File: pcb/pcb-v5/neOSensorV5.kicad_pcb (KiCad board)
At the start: 2 copper layers, 49.5 x 49.5 mm, 49 parts, among them J1 Conn_01x04, J2 Conn_01x04, J3 Conn_01x05, J4 Conn_01x05, J5 Conn_01x05, J6 Conn_01x06, Q1 2N7002, SW1 clear, SW2 +, SW3 -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

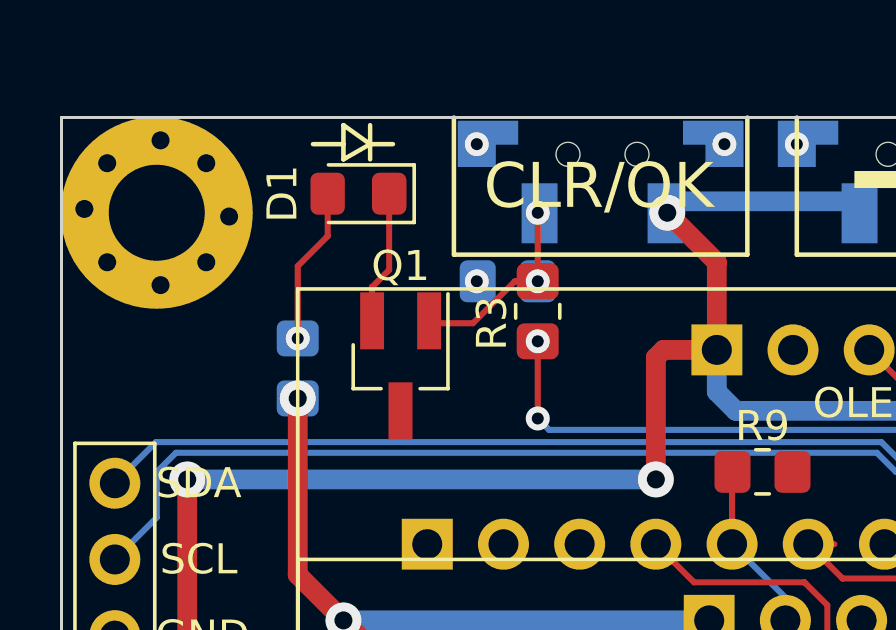
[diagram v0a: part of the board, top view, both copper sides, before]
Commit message: start mods for pcb v5.1
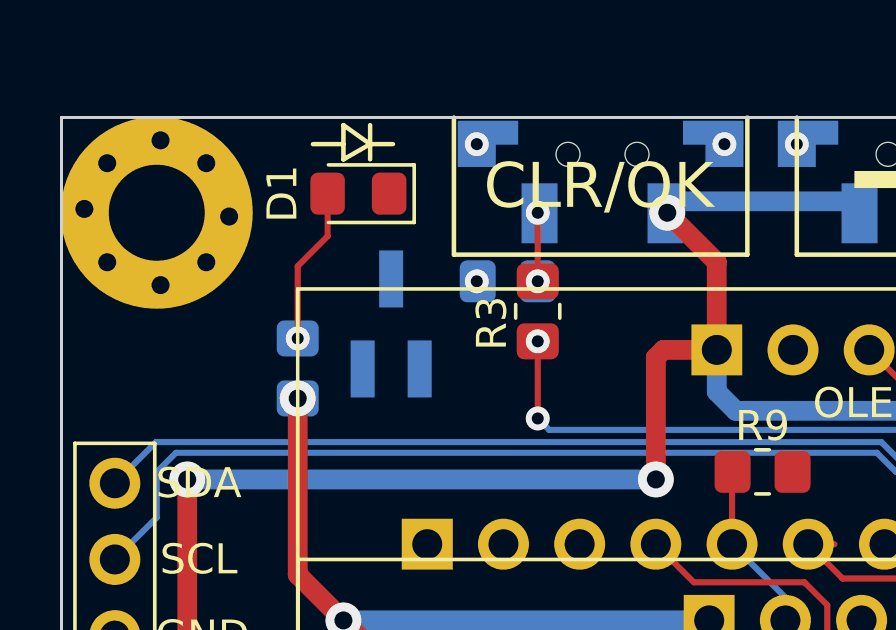
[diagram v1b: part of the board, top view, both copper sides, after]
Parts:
- Q1: moved to B.Cu
- moved Q1 1.43 mm to (36.4, 32.3), turned to 90 degrees
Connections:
- Q1 pad 2: Net-(D1-Pad1) -> GND
- Q1 pad 3: GND -> Net-(D1-Pad1)
- U3 pad 16: +3V3 -> Net-(U3-Pad16)
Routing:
- net Net-(D1-Pad1): track 4.47 -> 0.00 mm
- net Net-(Q1-Pad1): track 6.92 -> 2.69 mm
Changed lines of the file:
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@@
-(kicad_pcb (version 20171130) (host pcbnew 5.1.8-1.fc31)
+(kicad_pcb (version 20171130) (host pcbnew 5.1.5+dfsg1-2build2)
   (general
     (thickness 1.6)
     (drawings 71)
-    (tracks 381)
+    (tracks 374)
     (zones 0)
     (modules 49)
-    (nets 45)
+    (nets 46)
   )
   (page A4)
@@
     (32 B.Adhes user hide)
     (33 F.Adhes user hide)
-    (34 B.Paste user)
-    (35 F.Paste user)
+    (34 B.Paste user hide)
+    (35 F.Paste user hide)
     (36 B.SilkS user)
-    (37 F.SilkS user)
-    (38 B.Mask user)
-    (39 F.Mask user)
-    (40 Dwgs.User user)
+    (37 F.SilkS user hide)
+    (38 B.Mask user hide)
+    (39 F.Mask user hide)
+    (40 Dwgs.User user hide)
     (41 Cmts.User user hide)
     (42 Eco1.User user hide)
@@
   (net 43 "Net-(U3-Pad1)")
   (net 44 "Net-(D1-Pad2)")
+  (net 45 "Net-(U3-Pad16)")
   (net_class Default "This is the default net class."
     (clearance 0.1524)
@@
     (add_net "Net-(U3-Pad12)")
     (add_net "Net-(U3-Pad13)")
+    (add_net "Net-(U3-Pad16)")
     (add_net "Net-(U3-Pad21)")
     (add_net "Net-(U3-Pad22)")
@@
     (add_net GND)
   )
-  (module Package_TO_SOT_SMD:SOT-23_Handsoldering (layer F.Cu)
-    (at 36.703 33.679 270)
+  (module Package_TO_SOT_SMD:SOT-23_Handsoldering (layer B.Cu)
+    (at 36.388 32.282 90)
     (descr "SOT-23, Handsoldering")
     (tags SOT-23)
     (attr smd)
-    (fp_text reference Q1 (at -3.326 0 180) (layer F.SilkS)
-      (effects (font (size 1 1) (thickness 0.15)))
-    )
-    (fp_text value 2N7002 (at 0 2.5 90) (layer F.Fab)
-      (effects (font (size 1 1) (thickness 0.15)))
-    )
-    (fp_line (start 0.76 1.58) (end 0.76 0.65) (layer F.SilkS) (width 0.12))
-    (fp_line (start 0.76 -1.58) (end 0.76 -0.65) (layer F.SilkS) (width 0.12))
-    (fp_line (start -2.7 -1.75) (end 2.7 -1.75) (layer F.CrtYd) (width 0.05))
-    (fp_line (start 2.7 -1.75) (end 2.7 1.75) (layer F.CrtYd) (width 0.05))
-    (fp_line (start 2.7 1.75) (end -2.7 1.75) (layer F.CrtYd) (width 0.05))
-    (fp_line (start -2.7 1.75) (end -2.7 -1.75) (layer F.CrtYd) (width 0.05))
-    (fp_line (start 0.76 -1.58) (end -2.4 -1.58) (layer F.SilkS) (width 0.12))
-    (fp_line (start -0.7 -0.95) (end -0.7 1.5) (layer F.Fab) (width 0.1))
-    (fp_line (start -0.15 -1.52) (end 0.7 -1.52) (layer F.Fab) (width 0.1))
-    (fp_line (start -0.7 -0.95) (end -0.15 -1.52) (layer F.Fab) (width 0.1))
-    (fp_line (start 0.7 -1.52) (end 0.7 1.52) (layer F.Fab) (width 0.1))
-    (fp_line (start -0.7 1.52) (end 0.7 1.52) (layer F.Fab) (width 0.1))
-    (fp_line (start 0.76 1.58) (end -0.7 1.58) (layer F.SilkS) (width 0.12))
-    (fp_text user %R (at 0 0) (layer F.Fab)
-      (effects (font (size 0.5 0.5) (thickness 0.075)))
-    )
-    (pad 3 smd rect (at 1.5 0 270) (size 1.9 0.8) (layers F.Cu F.Paste F.Mask)
-      (net 1 GND))
-    (pad 2 smd rect (at -1.5 0.95 270) (size 1.9 0.8) (layers F.Cu F.Paste F.Mask)
+    (fp_text reference Q1 (at -3.326 0 180) (layer B.SilkS)
+      (effects (font (size 1 1) (thickness 0.15)) (justify mirror))
+    )
+    (fp_text value 2N7002 (at 0 -2.5 270) (layer B.Fab)
+      (effects (font (size 1 1) (thickness 0.15)) (justify mirror))
+    )
+    (fp_line (start 0.76 -1.58) (end 0.76 -0.65) (layer B.SilkS) (width 0.12))
+    (fp_line (start 0.76 1.58) (end 0.76 0.65) (layer B.SilkS) (width 0.12))
+    (fp_line (start -2.7 1.75) (end 2.7 1.75) (layer B.CrtYd) (width 0.05))
+    (fp_line (start 2.7 1.75) (end 2.7 -1.75) (layer B.CrtYd) (width 0.05))
+    (fp_line (start 2.7 -1.75) (end -2.7 -1.75) (layer B.CrtYd) (width 0.05))
+    (fp_line (start -2.7 -1.75) (end -2.7 1.75) (layer B.CrtYd) (width 0.05))
+    (fp_line (start 0.76 1.58) (end -2.4 1.58) (layer B.SilkS) (width 0.12))
+    (fp_line (start -0.7 0.95) (end -0.7 -1.5) (layer B.Fab) (width 0.1))
+    (fp_line (start -0.15 1.52) (end 0.7 1.52) (layer B.Fab) (width 0.1))
+    (fp_line (start -0.7 0.95) (end -0.15 1.52) (layer B.Fab) (width 0.1))
+    (fp_line (start 0.7 1.52) (end 0.7 -1.52) (layer B.Fab) (width 0.1))
+    (fp_line (start -0.7 -1.52) (end 0.7 -1.52) (layer B.Fab) (width 0.1))
+    (fp_line (start 0.76 -1.58) (end -0.7 -1.58) (layer B.SilkS) (width 0.12))
+    (fp_text user %R (at 0 0) (layer B.Fab)
+      (effects (font (size 0.5 0.5) (thickness 0.075)) (justify mirror))
+    )
+    (pad 3 smd rect (at 1.5 0 90) (size 1.9 0.8) (layers B.Cu B.Paste B.Mask)
       (net 6 "Net-(D1-Pad1)"))
-    (pad 1 smd rect (at -1.5 -0.95 270) (size 1.9 0.8) (layers F.Cu F.Paste F.Mask)
+    (pad 2 smd rect (at -1.5 -0.95 90) (size 1.9 0.8) (layers B.Cu B.Paste B.Mask)
+      (net 1 GND))
+    (pad 1 smd rect (at -1.5 0.95 90) (size 1.9 0.8) (layers B.Cu B.Paste B.Mask)
       (net 17 "Net-(Q1-Pad1)"))
     (model ${KISYS3DMOD}/Package_TO_SOT_SMD.3dshapes/SOT-23.wrl
@@
       (net 29 /ADC1_0))
     (pad 16 thru_hole circle (at -12.7 19.05 270) (size 1.7 1.7) (drill 1) (layers *.Cu *.Mask)
-      (net 3 +3V3))
+      (net 45 "Net-(U3-Pad16)"))
     (pad 15 thru_hole circle (at 12.7 19.05 270) (size 1.7 1.7) (drill 1) (layers *.Cu *.Mask)
       (net 5 /SW3))
@@
   (segment (start 71.12 37.592) (end 73.152 39.624) (width 0.2032) (layer F.Cu) (net 5))
   (segment (start 71.12 33.909) (end 71.12 37.592) (width 0.2032) (layer F.Cu) (net 5))
-  (segment (start 35.753 32.179) (end 35.753 31.049) (width 0.2032) (layer F.Cu) (net 6))
-  (segment (start 36.322 30.48) (end 36.322 27.94) (width 0.2032) (layer F.Cu) (net 6))
-  (segment (start 35.753 31.049) (end 36.322 30.48) (width 0.2032) (layer F.Cu) (net 6))
   (segment (start 62.992 37.306) (end 62.865 37.179) (width 0.2032) (layer F.Cu) (net 7))
   (segment (start 62.992 39.624) (end 62.992 37.306) (width 0.2032) (layer F.Cu) (net 7))
@@
   (segment (start 41.275 28.253) (end 41.334 28.194) (width 0.2032) (layer B.Cu) (net 17))
   (segment (start 41.275 28.575) (end 41.275 28.253) (width 0.2032) (layer B.Cu) (net 17))
-  (segment (start 40.513 30.861) (end 41.275 30.861) (width 0.2032) (layer F.Cu) (net 17))
-  (segment (start 39.116 32.258) (end 40.513 30.861) (width 0.2032) (layer F.Cu) (net 17))
-  (segment (start 37.732 32.258) (end 37.653 32.179) (width 0.2032) (layer F.Cu) (net 17))
-  (segment (start 39.116 32.258) (end 37.732 32.258) (width 0.2032) (layer F.Cu) (net 17))
   (via (at 41.275 32.861) (size 0.8) (drill 0.4) (layers F.Cu B.Cu) (net 18))
   (segment (start 41.307 32.893) (end 41.275 32.861) (width 0.2032) (layer B.Cu) (net 18))

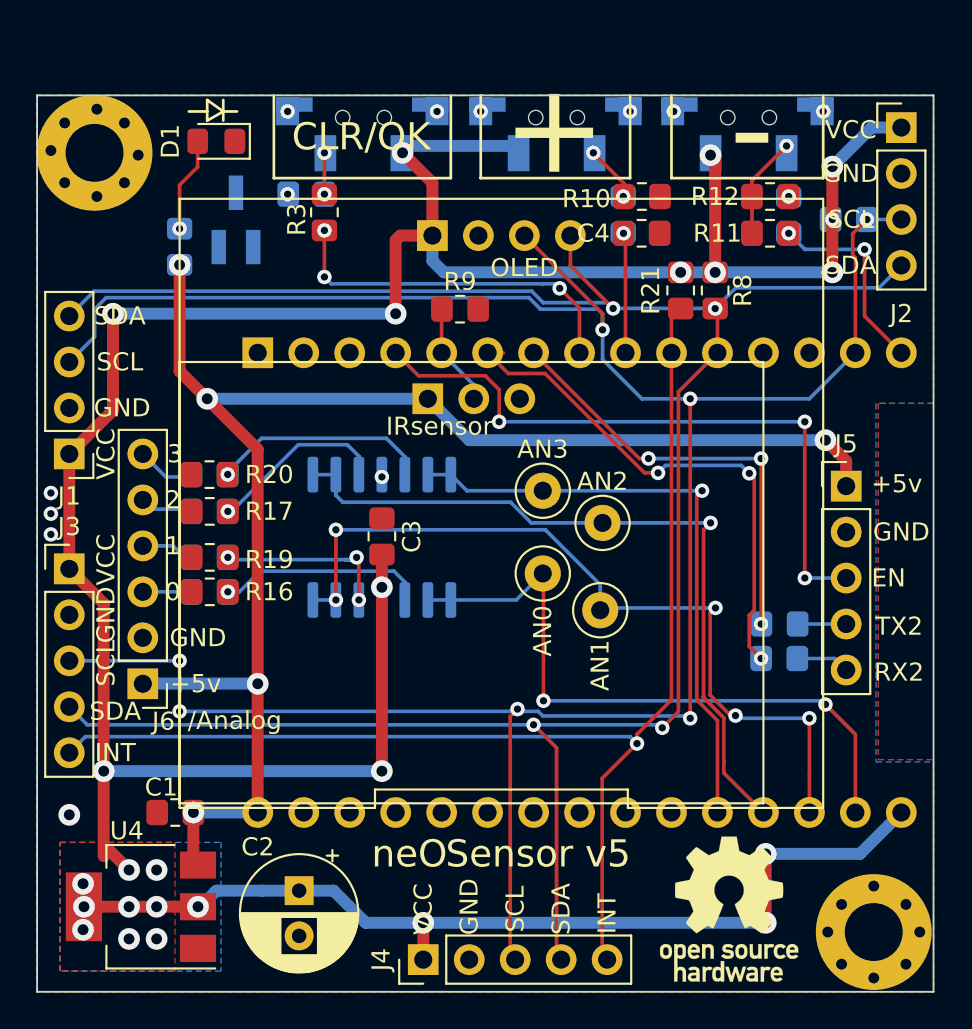
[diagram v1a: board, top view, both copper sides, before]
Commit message: updated pcb v5 layout
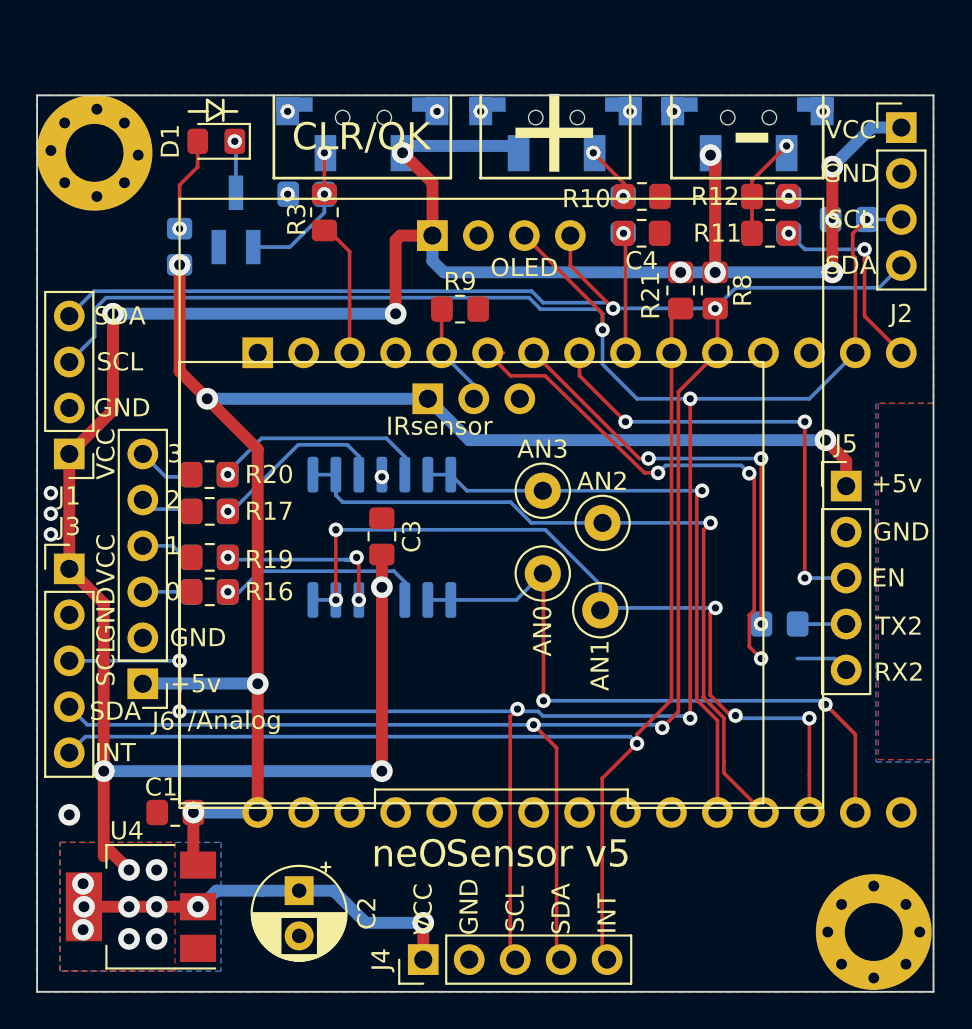
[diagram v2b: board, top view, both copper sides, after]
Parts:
- removed R6: 470, Resistor_SMD:R_0805_2012Metric_Pad1.20x1.40mm_HandSolder
- removed REF**: OSHW-Logo_7.5x8mm_SilkScreen, Symbol:OSHW-Logo_7.5x8mm_SilkScreen
- C2: value 470µF 6.3v -> 100µF 6.3v; footprint Capacitor_THT:CP_Radial_D6.3mm_P2.50mm -> Capacitor_THT:CP_Radial_D5.0mm_P2.50mm
- R1: value 68 -> 150
- R21: value 15K -> 15k
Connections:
- U3 pad 3: Net-(U3-Pad3) -> /LED
- U3 pad 4: /PM_EN -> Net-(U3-Pad4)
- U3 pad 6: Net-(R6-Pad2) -> /RX2
- U3 pad 8: /LED -> /PM_EN
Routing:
- net +3V3: track 189.1 -> 158.0 mm, vias 25 -> 23
- net Net-(R6-Pad2): track 29.2 -> 0.00 mm, vias 3 -> 0
- net /RX2: track 2.96 -> 32.1 mm, vias 0 -> 3
- net /LED: track 19.9 -> 7.47 mm, vias 3 -> 0
- net /PM_EN: track 36.1 -> 25.7 mm
- net Net-(Q1-Pad1): track 2.69 -> 8.43 mm
- net Net-(D1-Pad1): track 0.00 -> 2.87 mm, vias 0 -> 1

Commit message: update PCB V5.1
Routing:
- net /RX2: track 32.1 -> 34.1 mm
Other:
- board text added: "IR"
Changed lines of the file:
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@@
-(kicad_pcb (version 20171130) (host pcbnew 5.1.8-1.fc31)
+(kicad_pcb (version 20171130) (host pcbnew 5.1.5+dfsg1-2build2)
   (general
     (thickness 1.6)
-    (drawings 71)
-    (tracks 364)
+    (drawings 78)
+    (tracks 365)
     (zones 0)
     (modules 47)
@@
     (33 F.Adhes user hide)
     (34 B.Paste user hide)
-    (35 F.Paste user hide)
+    (35 F.Paste user)
     (36 B.SilkS user hide)
     (37 F.SilkS user)
     (38 B.Mask user hide)
-    (39 F.Mask user hide)
+    (39 F.Mask user)
     (40 Dwgs.User user hide)
     (41 Cmts.User user hide)
@@
     (descr "CP, Radial series, Radial, pin pitch=2.50mm, , diameter=5mm, Electrolytic Capacitor")
     (tags "CP Radial series Radial pin pitch 2.50mm  diameter 5mm Electrolytic Capacitor")
-    (fp_text reference C2 (at 1.25 -3.75 90) (layer F.SilkS)
+    (fp_text reference C2 (at -1.524 2.54 180) (layer F.SilkS)
       (effects (font (size 1 1) (thickness 0.15)))
     )
@@
     (tags "resistor handsolder")
     (attr smd)
-    (fp_text reference R9 (at 0 1.524) (layer F.SilkS)
+    (fp_text reference R9 (at 2.54 -0.127 90) (layer F.SilkS)
       (effects (font (size 1 1) (thickness 0.15)))
     )
@@
     )
   )
+  (gr_text GND (at 52.324 44.196) (layer F.SilkS)
+    (effects (font (size 1 1) (thickness 0.15)))
+  )
+  (gr_text IR (at 49.53 44.196) (layer F.SilkS)
+    (effects (font (size 1 1) (thickness 0.15)))
+  )
+  (gr_text +5v (at 46.736 44.196) (layer F.SilkS)
+    (effects (font (size 1 1) (thickness 0.15)))
+  )
+  (gr_text SDA (at 54.864 35.56 90) (layer F.SilkS)
+    (effects (font (size 1 1) (thickness 0.15)))
+  )
+  (gr_text SCL (at 52.324 35.56 90) (layer F.SilkS)
+    (effects (font (size 1 1) (thickness 0.15)))
+  )
+  (gr_text GND (at 50.038 35.052) (layer F.SilkS)
+    (effects (font (size 1 1) (thickness 0.15)))
+  )
+  (gr_text VCC (at 46.736 35.052) (layer F.SilkS)
+    (effects (font (size 1 1) (thickness 0.15)))
+  )
   (dimension 53.975 (width 0.15) (layer Dwgs.User)
     (gr_text "53,975 mm" (at 52.3875 77.246) (layer Dwgs.User)
@@
     (arrow2b (pts (xy 28.575 22.352) (xy 29.701504 21.765579)))
   )
-  (gr_text AN3 (at 53.34 44.958) (layer F.SilkS)
-    (effects (font (size 1 1) (thickness 0.15)))
-  )
-  (gr_text AN2 (at 56.642 46.736) (layer F.SilkS)
+  (gr_text AN3 (at 51.054 47.244 90) (layer F.SilkS)
+    (effects (font (size 1 1) (thickness 0.15)))
+  )
+  (gr_text AN2 (at 56.642 45.974 90) (layer F.SilkS)
     (effects (font (size 1 1) (thickness 0.15)))
   )
@@
     (effects (font (size 3 3) (thickness 0.3)) (justify mirror))
   )
-  (gr_text OLED (at 52.324 34.925) (layer F.SilkS)
-    (effects (font (size 1 1) (thickness 0.15)))
-  )
-  (gr_text IRsensor (at 47.625 43.688) (layer F.SilkS)
+  (gr_text OLED (at 51.054 31.496) (layer F.SilkS)
+    (effects (font (size 1 1) (thickness 0.15)))
+  )
+  (gr_text IRsensor (at 56.642 42.164) (layer F.SilkS)
     (effects (font (size 1 1) (thickness 0.15)))
   )
@@
   (segment (start 69.469 56.515) (end 70.104 57.15) (width 0.2032) (layer B.Cu) (net 10))
   (segment (start 67.405 56.515) (end 69.469 56.515) (width 0.2032) (layer B.Cu) (net 10))
-  (segment (start 67.421 54.61) (end 70.104 54.61) (width 0.2032) (layer B.Cu) (net 11))
-  (via (at 67.818 43.434) (size 0.8) (drill 0.4) (layers F.Cu B.Cu) (net 12))
-  (via (at 67.818 52.07) (size 0.8) (drill 0.4) (layers F.Cu B.Cu) (net 12))
-  (segment (start 67.818 43.434) (end 67.818 52.07) (width 0.2032) (layer F.Cu) (net 12))
-  (segment (start 67.818 52.07) (end 70.104 52.07) (width 0.2032) (layer B.Cu) (net 12))
-  (segment (start 31.242 52.832) (end 33.671 52.832) (width 0.2032) (layer B.Cu) (net 13))
-  (segment (start 32.909 50.292) (end 33.671 51.054) (width 0.2032) (layer B.Cu) (net 14))
-  (segment (start 31.242 50.292) (end 32.909 50.292) (width 0.2032) (layer B.Cu) (net 14))
-  (segment (start 31.242 47.752) (end 31.75 48.26) (width 0.2032) (layer B.Cu) (net 15))
-  (segment (start 31.75 48.26) (end 33.671 48.26) (width 0.2032) (layer B.Cu) (net 15))
-  (segment (start 32.512 46.482) (end 33.671 46.482) (width 0.2032) (layer B.Cu) (net 16))
-  (segment (start 31.242 45.212) (end 32.512 46.482) (width 0.2032) (layer B.Cu) (net 16))
-  (via (at 41.275 30.861) (size 0.8) (drill 0.4) (layers F.Cu B.Cu) (net 17))
-  (via (at 41.275 28.575) (size 0.8) (drill 0.4) (layers F.Cu B.Cu) (net 17))
-  (segment (start 41.275 30.861) (end 41.275 28.575) (width 0.2032) (layer F.Cu) (net 17))
-  (segment (start 41.275 28.253) (end 41.334 28.194) (width 0.2032) (layer B.Cu) (net 17))
-  (segment (start 41.275 28.575) (end 41.275 28.253) (width 0.2032) (layer B.Cu) (net 17))
-  (via (at 59.182 45.466) (size 0.8) (drill 0.4) (layers F.Cu B.Cu) (net 19))
-  (segment (start 52.832 39.624) (end 58.674 45.466) (width 0.2032) (layer F.Cu) (net 19))
-  (segment (start 58.674 45.466) (end 59.182 45.466) (width 0.2032) (layer F.Cu) (net 19))
-  (via (at 65.405 45.466) (size 0.8) (drill 0.4) (layers F.Cu B.Cu) (net 19))
-  (segment (start 59.182 45.466) (end 65.405 45.466) (width 0.2032) (layer B.Cu) (net 19))
-  (segment (start 65.405 45.466) (end 65.405 54.61) (width 0.2032) (layer F.Cu) (net 19))
-  (via (at 65.405 54.61) (size 0.8) (drill 0.4) (layers F.Cu B.Cu) (net 19))
   (via (at 65.405 56.515) (size 0.8) (drill 0.4) (layers F.Cu B.Cu) (net 10))
   (segment (start 50.292 39.624) (end 51.163922 39.624) (width 0.2032) (layer F.Cu) (net 10))
@@
   (segment (start 59.710297 46.258446) (end 58.963538 46.258446) (width 0.2032) (layer F.Cu) (net 10))
   (segment (start 58.963538 46.258446) (end 53.467 40.894) (width 0.2032) (layer F.Cu) (net 10))
+  (segment (start 67.405 56.515) (end 65.405 56.515) (width 0.2032) (layer B.Cu) (net 10))
+  (segment (start 67.421 54.61) (end 70.104 54.61) (width 0.2032) (layer B.Cu) (net 11))
+  (via (at 67.818 43.434) (size 0.8) (drill 0.4) (layers F.Cu B.Cu) (net 12))
+  (via (at 67.818 52.07) (size 0.8) (drill 0.4) (layers F.Cu B.Cu) (net 12))
+  (segment (start 67.818 43.434) (end 67.818 52.07) (width 0.2032) (layer F.Cu) (net 12))
+  (segment (start 67.818 52.07) (end 70.104 52.07) (width 0.2032) (layer B.Cu) (net 12))
   (segment (start 57.912 43.434) (end 67.818 43.434) (width 0.2032) (layer B.Cu) (net 12))
   (via (at 57.912 43.434) (size 0.8) (drill 0.4) (layers F.Cu B.Cu) (net 12))
   (segment (start 55.372 40.894) (end 57.912 43.434) (width 0.2032) (layer F.Cu) (net 12))
   (segment (start 55.372 39.624) (end 55.372 40.894) (width 0.2032) (layer F.Cu) (net 12))
+  (segment (start 31.242 52.832) (end 33.671 52.832) (width 0.2032) (layer B.Cu) (net 13))
+  (segment (start 32.909 50.292) (end 33.671 51.054) (width 0.2032) (layer B.Cu) (net 14))
+  (segment (start 31.242 50.292) (end 32.909 50.292) (width 0.2032) (layer B.Cu) (net 14))
+  (segment (start 31.242 47.752) (end 31.75 48.26) (width 0.2032) (layer B.Cu) (net 15))
+  (segment (start 31.75 48.26) (end 33.671 48.26) (width 0.2032) (layer B.Cu) (net 15))
+  (segment (start 32.512 46.482) (end 33.671 46.482) (width 0.2032) (layer B.Cu) (net 16))
+  (segment (start 31.242 45.212) (end 32.512 46.482) (width 0.2032) (layer B.Cu) (net 16))
+  (via (at 41.275 30.861) (size 0.8) (drill 0.4) (layers F.Cu B.Cu) (net 17))
+  (via (at 41.275 28.575) (size 0.8) (drill 0.4) (layers F.Cu B.Cu) (net 17))
+  (segment (start 41.275 30.861) (end 41.275 28.575) (width 0.2032) (layer F.Cu) (net 17))
+  (segment (start 41.275 28.253) (end 41.334 28.194) (width 0.2032) (layer B.Cu) (net 17))
+  (segment (start 41.275 28.575) (end 41.275 28.253) (width 0.2032) (layer B.Cu) (net 17))
   (segment (start 37.338 33.782) (end 39.37 33.782) (width 0.2032) (layer B.Cu) (net 17))
   (segment (start 41.275 31.877) (end 41.275 30.861) (width 0.2032) (layer B.Cu) (net 17))
@@
   (segment (start 42.672 34.036) (end 42.672 39.624) (width 0.2032) (layer F.Cu) (net 18))
   (segment (start 41.497 32.861) (end 42.672 34.036) (width 0.2032) (layer F.Cu) (net 18))
+  (via (at 59.182 45.466) (size 0.8) (drill 0.4) (layers F.Cu B.Cu) (net 19))
+  (segment (start 52.832 39.624) (end 58.674 45.466) (width 0.2032) (layer F.Cu) (net 19))
+  (segment (start 58.674 45.466) (end 59.182 45.466) (width 0.2032) (layer F.Cu) (net 19))
+  (via (at 65.405 45.466) (size 0.8) (drill 0.4) (layers F.Cu B.Cu) (net 19))
+  (segment (start 59.182 45.466) (end 65.405 45.466) (width 0.2032) (layer B.Cu) (net 19))
+  (segment (start 65.405 45.466) (end 65.405 54.61) (width 0.2032) (layer F.Cu) (net 19))
+  (via (at 65.405 54.61) (size 0.8) (drill 0.4) (layers F.Cu B.Cu) (net 19))
   (via (at 57.785 30.988) (size 0.8) (drill 0.4) (layers F.Cu B.Cu) (net 20))
   (via (at 56.134 28.575) (size 0.8) (drill 0.4) (layers F.Cu B.Cu) (net 20))
